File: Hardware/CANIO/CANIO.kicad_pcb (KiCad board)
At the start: 2 copper layers, 68.2 x 48.5 mm, 31 parts, among them J102 Tag Connect, J103 PWR, J201 CAN, J202 CAN, P101 USB_C_Plug_USB2.0, SW101 RESET, U101 ATmega16U2, U201 MCP25625-x-SS, Y101 DNP, Y202 Crystal_GND24

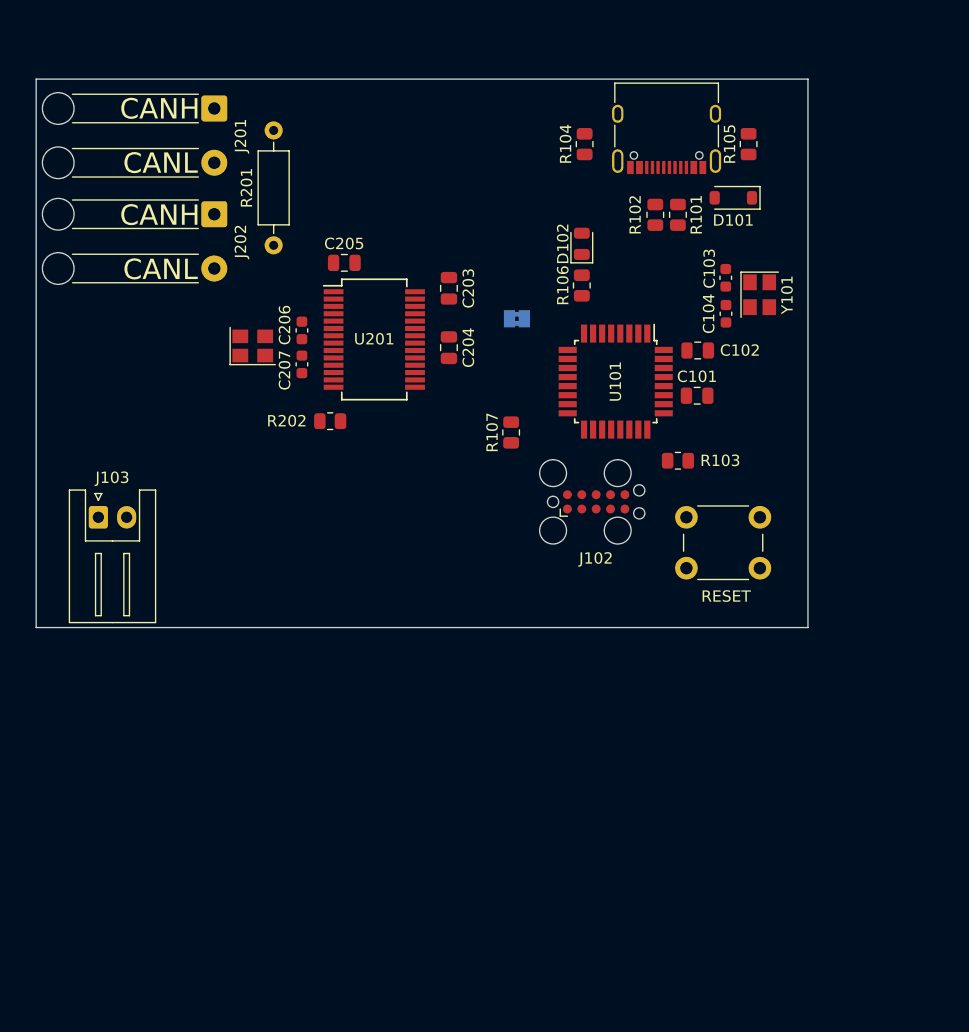
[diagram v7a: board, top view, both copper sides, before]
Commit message: Design improvements, multilayer and more
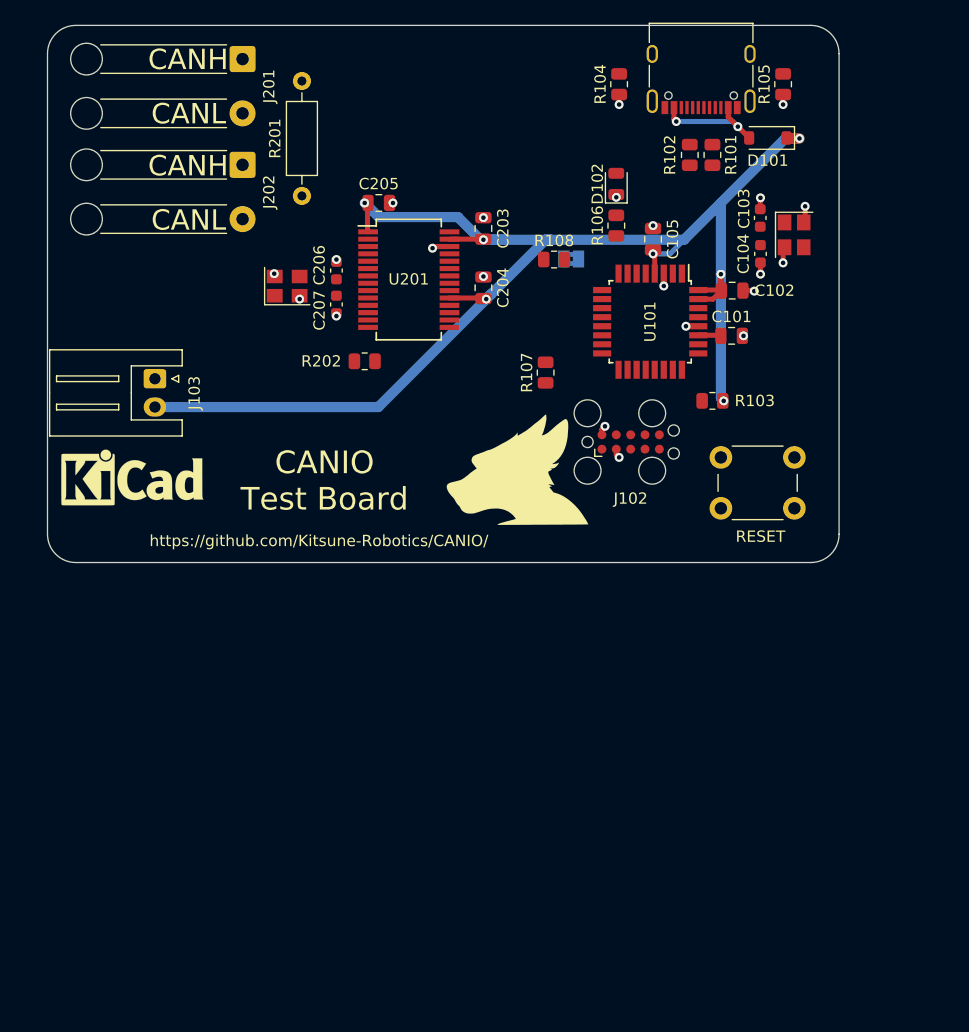
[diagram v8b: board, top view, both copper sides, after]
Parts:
- added C105: 100nF, Capacitor_SMD:C_0805_2012Metric, F.Cu at (28.6, -26.1)
- added G***: LOGO, KenwoodFox:KITSUNE_LOGO, F.Cu at (16.5, -5.75)
- added G***: LOGO, CANIO:QRCODE, B.Cu at (2.75, -4.75)
- added R108: 100R, Resistor_SMD:R_0805_2012Metric, F.Cu at (19.8, -24.3)
- added REF**: KiCad-Logo_5mm_SilkScreen, Symbol:KiCad-Logo_5mm_SilkScreen, F.Cu at (-17.5, -4.50)
- added REF**: OSHW-Logo2_9.8x8mm_SilkScreen, Symbol:OSHW-Logo2_9.8x8mm_SilkScreen, B.Cu at (-8.25, -4.50)
- moved J103 13.2 mm to (-15.5, -13.8), turned to -90 degrees
- moved JP101 7.15 mm to (21.3, -24.3), turned to 0 degrees
- moved C103 6.11 mm to (38.0, -28.0)
- moved D101 6.11 mm to (38.7, -35.0)
- moved Y101 6.11 mm to (41.0, -26.5)
- moved C203 6.11 mm to (13.6, -27.0)
- moved C204 6.11 mm to (13.6, -21.8)
- moved C205 6.11 mm to (4.30, -29.3)
- moved C206 6.11 mm to (0.55, -23.3)
- moved D102 6.11 mm to (25.3, -31.0)
- moved R102 6.11 mm to (31.8, -33.5)
- moved R104 6.11 mm to (25.6, -39.8)
- moved R106 6.11 mm to (25.3, -27.3)
- moved U101 6.11 mm to (28.3, -18.8)
- moved Y202 6.11 mm to (-3.80, -21.9)
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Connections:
- JP101 pad 1: /CLKOUT -> Net-(JP101-A)
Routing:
- net +5V: track 0.00 -> 132.9 mm, vias 0 -> 8
- net GND: track 0.00 -> 12.3 mm, vias 0 -> 21
- net Net-(D101-A): track 0.00 -> 10.4 mm, vias 0 -> 2
- net Net-(U101-UCAP): track 0.00 -> 2.02 mm
- added copper zone on In1.Cu, net GND
- added copper zone on In2.Cu, net GND
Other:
- board size 68.2 x 48.5 mm -> 70 x 47.5 mm
- copper layers 2 -> 4
- board text added: "CANIO Test Board"
- board text added: "https://github.com/Kitsune-Robotics/CANIO/"
